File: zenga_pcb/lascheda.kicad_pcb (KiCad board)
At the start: 2 copper layers, 175.7 x 167.8 mm, 50 parts

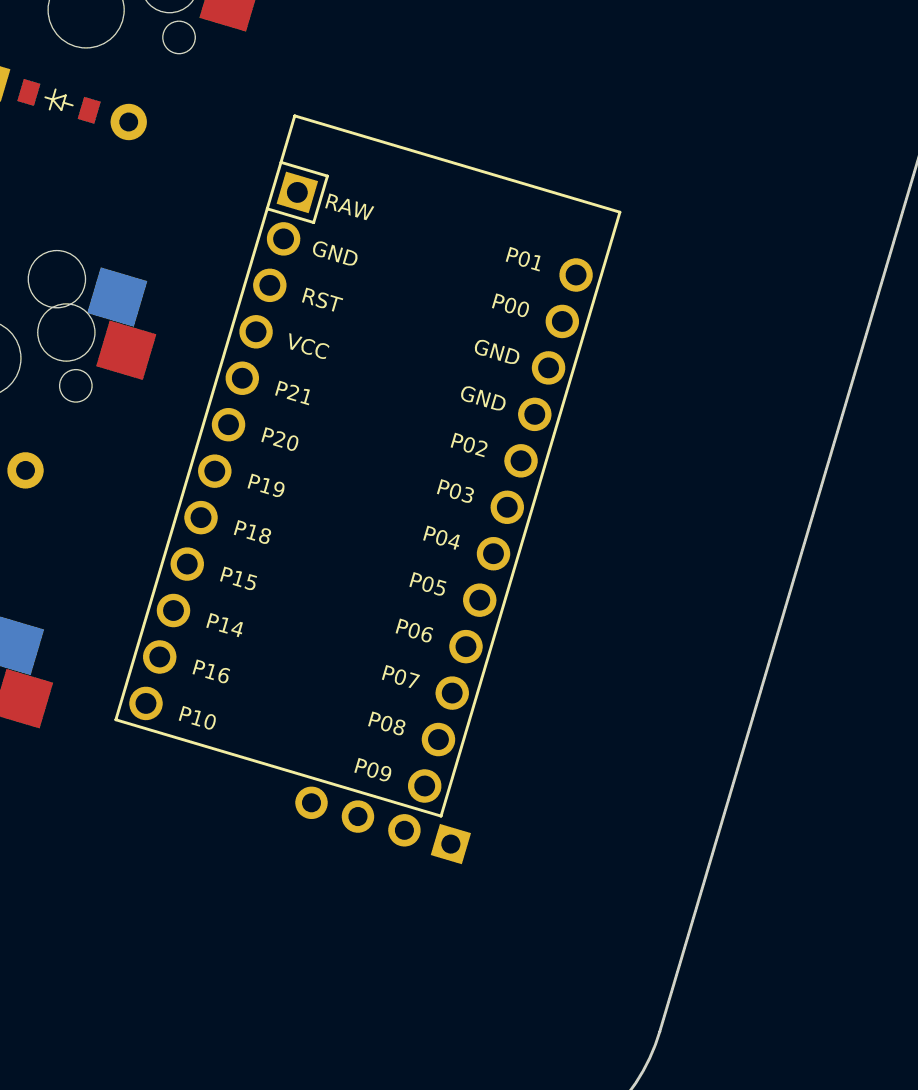
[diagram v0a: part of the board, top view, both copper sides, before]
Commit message: Move to rp2040zero
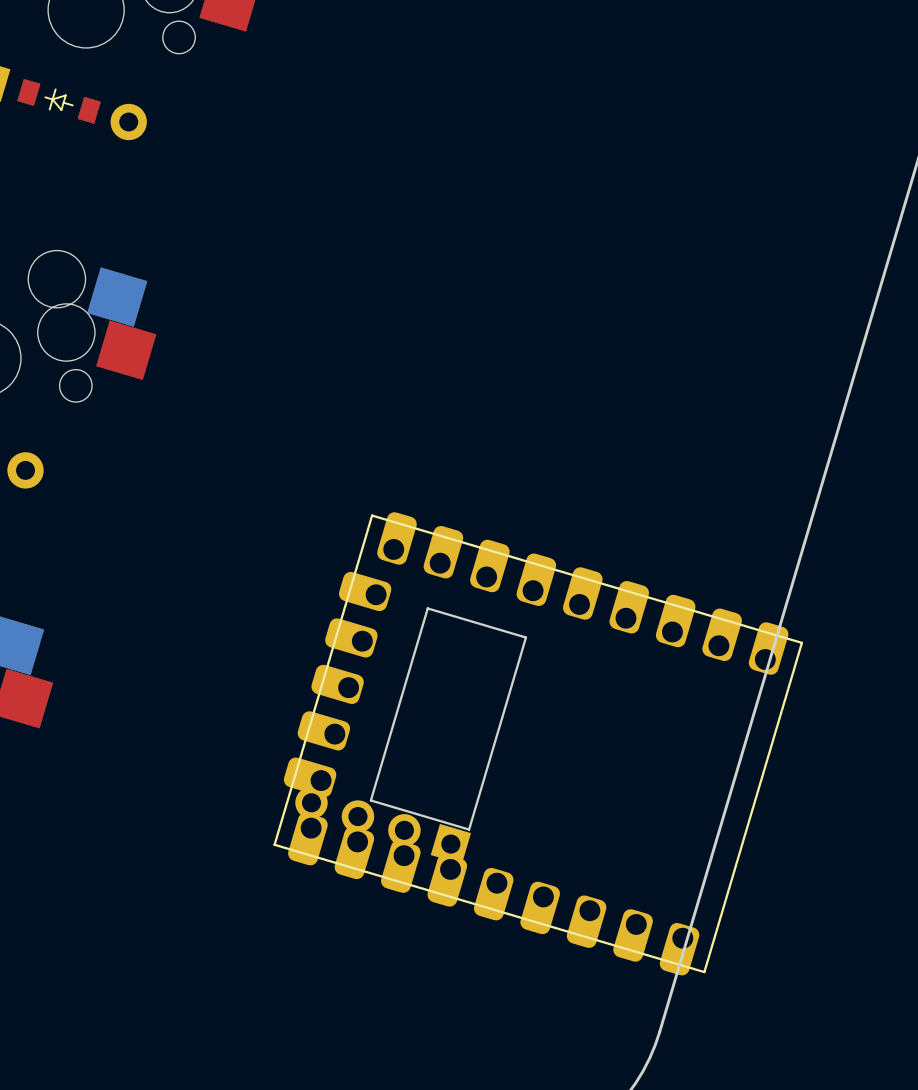
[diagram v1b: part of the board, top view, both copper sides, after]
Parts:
- removed MCU1: , ProMicro
- added RP2040Zero1: , RP2040-Zero, F.Cu at (202.8, 114.6)

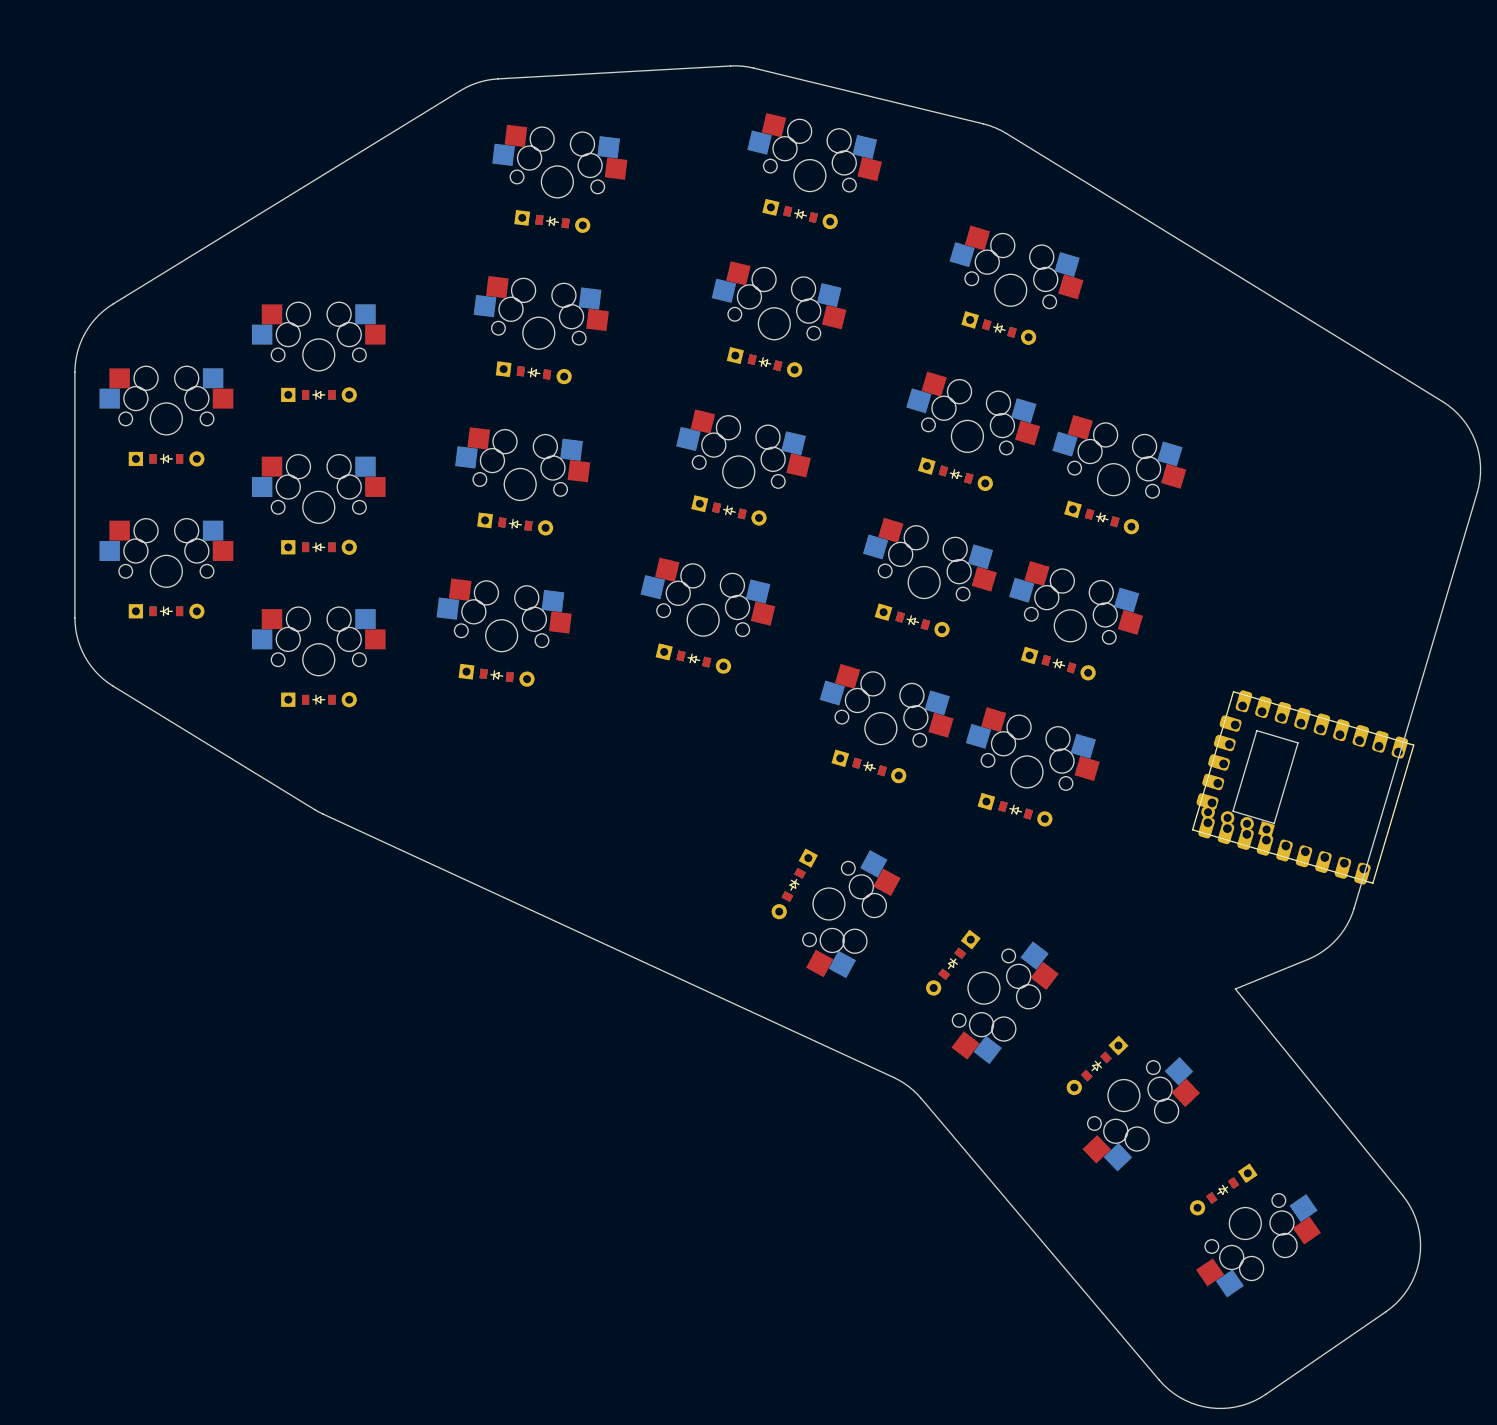
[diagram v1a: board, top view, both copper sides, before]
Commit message: Start create nets
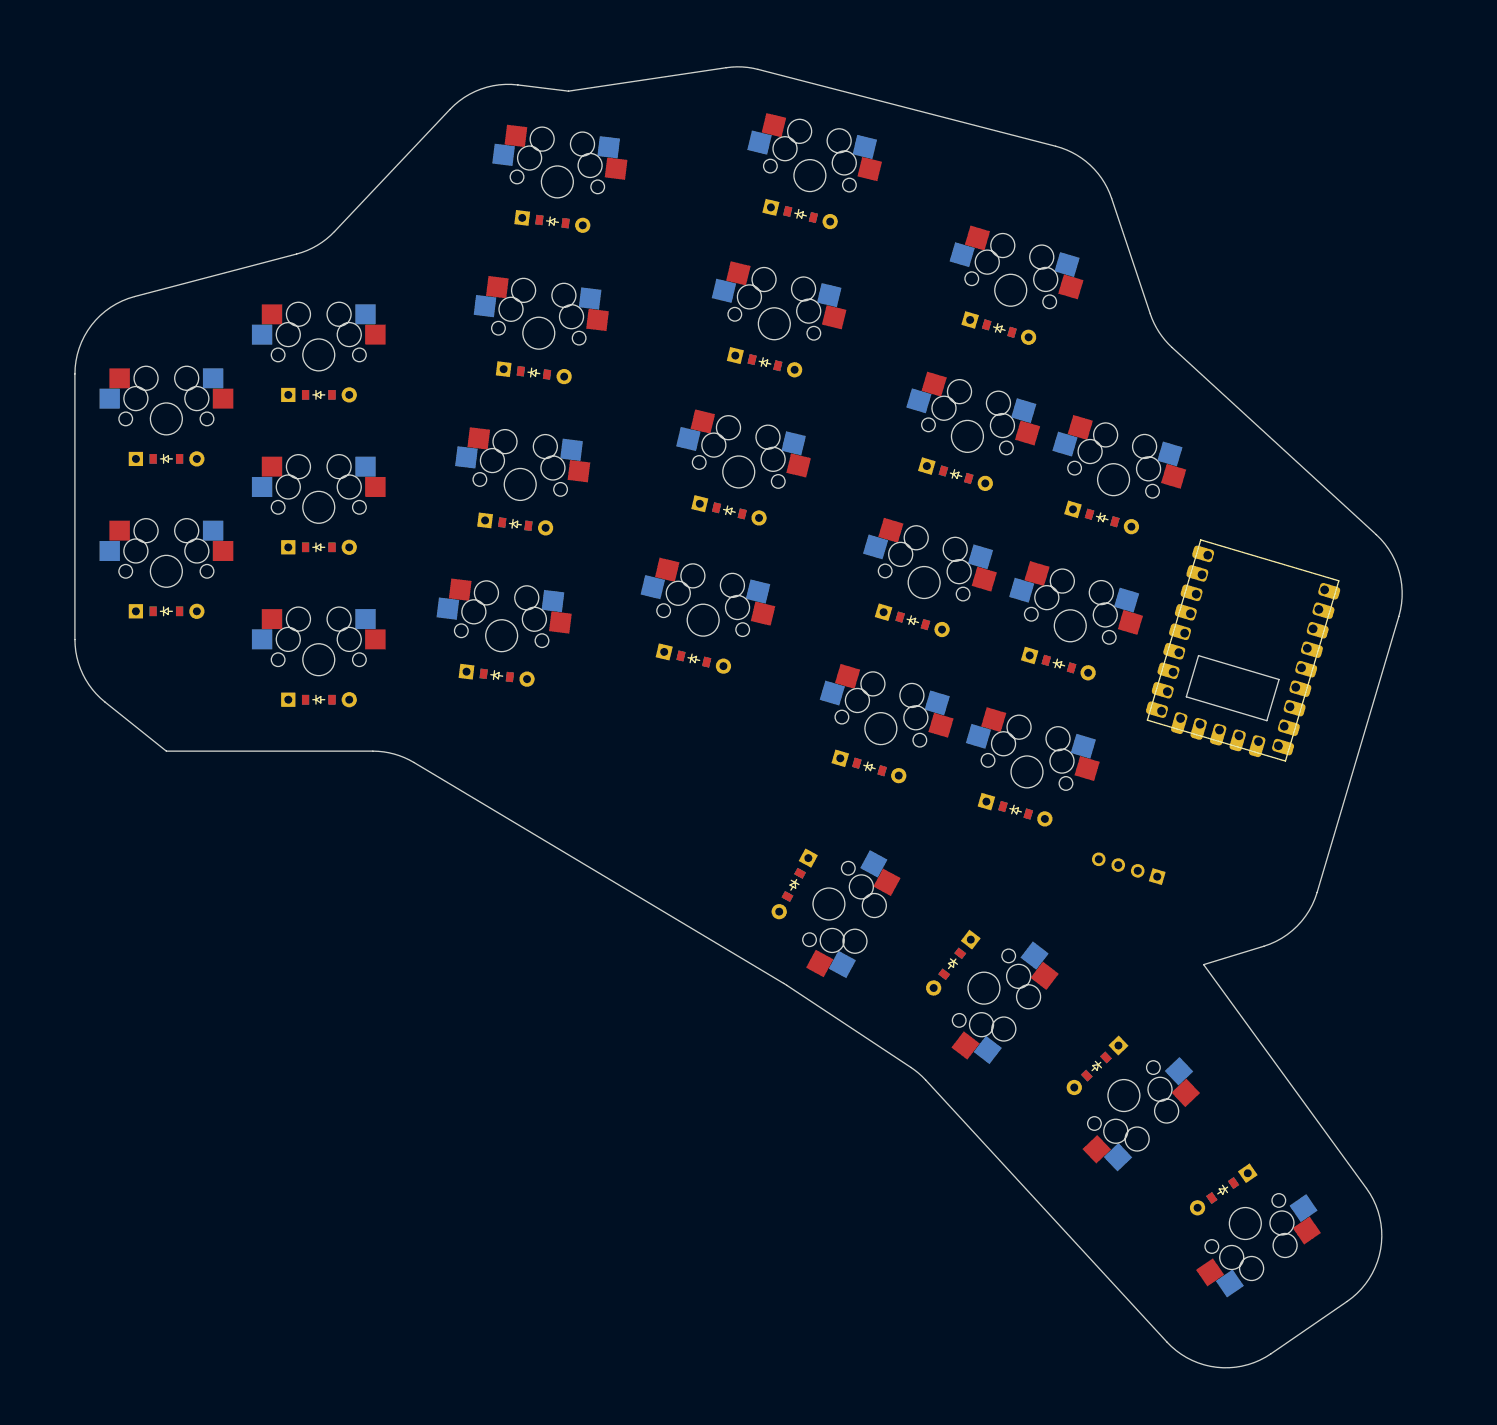
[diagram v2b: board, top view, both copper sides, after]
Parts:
- moved OLED1 14.9 mm to (184.0, 137.9)
- moved RP2040Zero1 12.8 mm to (191.2, 120.1), turned to -16.5 degrees
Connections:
- D1 pad 1: (no net) -> GP28
- D10 pad 1: (no net) -> GP26
- D11 pad 1: (no net) -> GP27
- D12 pad 1: (no net) -> GP28
- D13 pad 1: (no net) -> GP29
- D14 pad 1: (no net) -> GP26
- D15 pad 1: (no net) -> GP27
- D16 pad 1: (no net) -> GP28
- D17 pad 1: (no net) -> GP29
- D18 pad 1: (no net) -> GP26
- D19 pad 1: (no net) -> GP27
- D2 pad 1: (no net) -> GP29
- D20 pad 1: (no net) -> GP28
- D3 pad 1: (no net) -> GP27
- D4 pad 1: (no net) -> GP28
- D5 pad 1: (no net) -> GP29
- D6 pad 1: (no net) -> GP26
- D7 pad 1: (no net) -> GP27
- D8 pad 1: (no net) -> GP28
- D9 pad 1: (no net) -> GP29
- OLED1 pad 2: VCC -> P3V3
- OLED1 pad 3: P3 -> GP1
- OLED1 pad 4: P2 -> GP0
- S21 pad 1: (no net) -> GP5
- S22 pad 1: (no net) -> GP4
- S23 pad 1: (no net) -> GP3
- S24 pad 1: (no net) -> GP2
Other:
- board size 175.7 x 167.8 mm -> 165.9 x 162.6 mm

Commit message: Kicad 8
Set Kicad 8 template in the ergogen config
Fix more column overlap names
Save some images in the repo
Save a manually crafter PCB KiCAD file
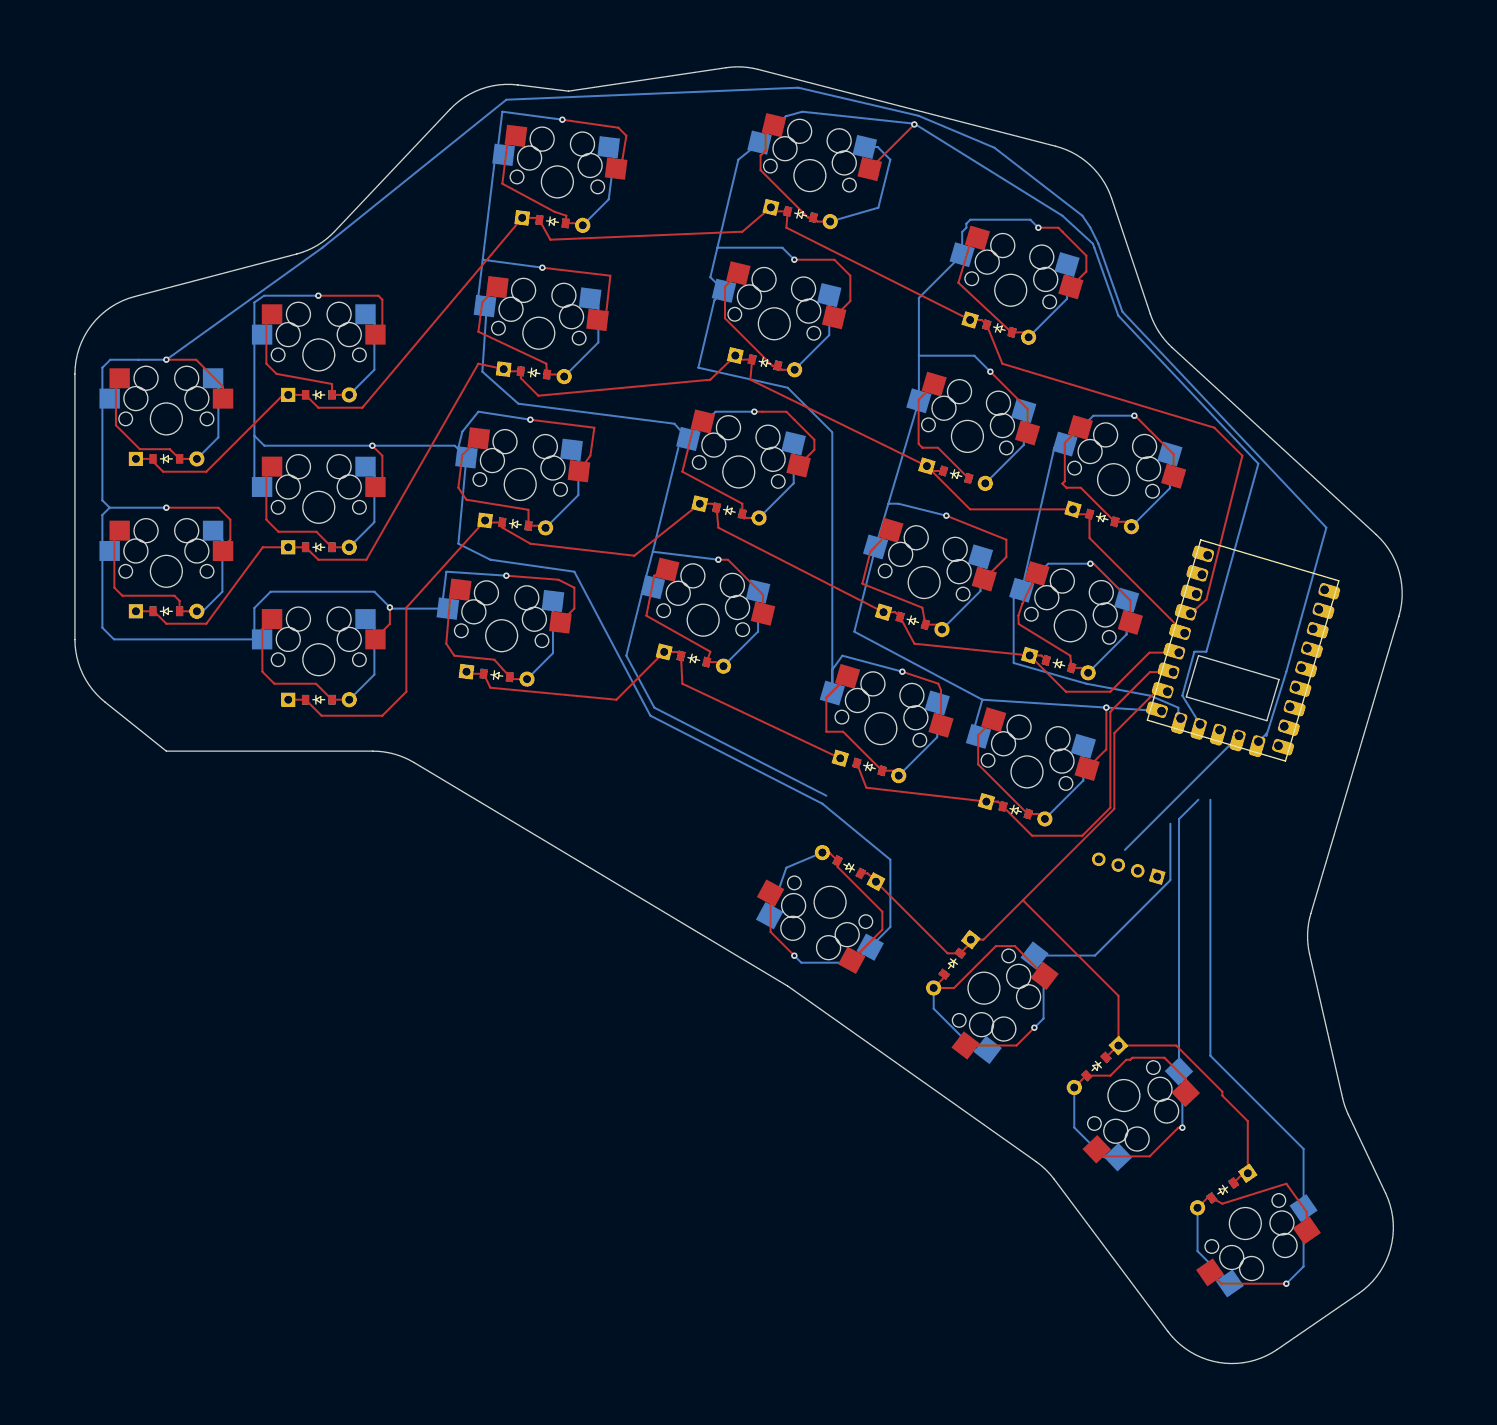
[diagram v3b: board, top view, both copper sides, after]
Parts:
- moved D21 7.27 mm to (155.4, 137.9), turned to 151.5 degrees
- moved S21 0.26 mm to (153.0, 142.3), turned to 151.5 degrees
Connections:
- net inner_mod renamed indexinner_mod
- net inner_top renamed pinkyinner_top
- net main_inner renamed thumbmain_thumbouter
- net main_moreinner renamed thumbmain_thumbmoreouter
- net main_moreouter renamed thumbmain_thumbmoreinner
- net main_outer renamed thumbmain_thumbinner
- net outer_bottom renamed indexouter_bottom
- net outer_mod renamed indexouter_mod
- D1 pad 2: outer_home -> pinkyouter_home
- D10 pad 2: main_mod -> middlemain_mod
- D11 pad 2: main_bottom -> middlemain_bottom
- D12 pad 2: main_home -> middlemain_home
- D13 pad 2: main_top -> middlemain_top
- D16 pad 2: outer_home -> indexouter_home
- D17 pad 2: outer_top -> indexouter_top
- D19 pad 2: inner_bottom -> indexinner_bottom
- D2 pad 2: outer_top -> pinkyouter_top
- D20 pad 2: inner_home -> indexinner_home
- D21 pad 1: (no net) -> GP15
- D22 pad 1: (no net) -> GP15
- D23 pad 1: (no net) -> GP15
- D24 pad 1: (no net) -> GP15
- D3 pad 2: inner_bottom -> pinkyinner_bottom
- D4 pad 2: inner_home -> pinkyinner_home
- D6 pad 2: main_mod -> ringmain_mod
- D7 pad 2: main_bottom -> ringmain_bottom
- D8 pad 2: main_home -> ringmain_home
- D9 pad 2: main_top -> ringmain_top
- S1 pad 1: (no net) -> GP9
- S1 pad 2: outer_home -> pinkyouter_home
- S10 pad 1: (no net) -> GP11
- S10 pad 2: main_mod -> middlemain_mod
- S11 pad 1: (no net) -> GP11
- S11 pad 2: main_bottom -> middlemain_bottom
- S12 pad 1: (no net) -> GP12
- S12 pad 2: main_home -> middlemain_home
- S13 pad 1: (no net) -> GP12
- S13 pad 2: main_top -> middlemain_top
- S14 pad 1: (no net) -> GP12
- S15 pad 1: (no net) -> GP14
- S16 pad 1: (no net) -> GP14
- S16 pad 2: outer_home -> indexouter_home
- S17 pad 1: (no net) -> GP14
- S17 pad 2: outer_top -> indexouter_top
- S18 pad 1: (no net) -> GP14
- S19 pad 1: (no net) -> GP13
- S19 pad 2: inner_bottom -> indexinner_bottom
- S2 pad 1: (no net) -> GP9
- S2 pad 2: outer_top -> pinkyouter_top
- S20 pad 1: (no net) -> GP13
- S20 pad 2: inner_home -> indexinner_home
- S21 pad 1: GP5 -> GP10
- S22 pad 1: GP4 -> GP11
- S23 pad 1: GP3 -> GP12
- S24 pad 1: GP2 -> GP13
- S3 pad 1: (no net) -> GP9
- S3 pad 2: inner_bottom -> pinkyinner_bottom
- S4 pad 1: (no net) -> GP10
- S4 pad 2: inner_home -> pinkyinner_home
- S5 pad 1: (no net) -> GP10
- S6 pad 1: (no net) -> GP9
- S6 pad 2: main_mod -> ringmain_mod
- S7 pad 1: (no net) -> GP10
- S7 pad 2: main_bottom -> ringmain_bottom
- S8 pad 1: (no net) -> GP11
- S8 pad 2: main_home -> ringmain_home
- S9 pad 1: (no net) -> GP11
- S9 pad 2: main_top -> ringmain_top
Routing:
- net GP9: track 0.00 -> 364.0 mm, vias 0 -> 4
- net GP12: track 0.00 -> 311.4 mm, vias 0 -> 4
- net GP11: track 0.00 -> 243.4 mm, vias 0 -> 5
- net GP10: track 0.00 -> 239.8 mm, vias 0 -> 4
- net GP29: track 0.00 -> 190.2 mm
- net GP28: track 0.00 -> 173.1 mm
- net GP14: track 0.00 -> 170.1 mm, vias 0 -> 4
- net GP13: track 0.00 -> 169.1 mm, vias 0 -> 3
- net GP27: track 0.00 -> 145.9 mm
- net GP15: track 0.00 -> 116.3 mm
- net GP26: track 0.00 -> 115.1 mm
- net middlemain_top: track 0.00 -> 34.0 mm
- net ringmain_bottom: track 0.00 -> 32.8 mm
- net pinkyouter_home: track 0.00 -> 32.0 mm
- net indexouter_bottom: track 0.00 -> 31.5 mm
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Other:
- board size 165.9 x 162.6 mm -> 165.9 x 162.1 mm
- net class Default removed
